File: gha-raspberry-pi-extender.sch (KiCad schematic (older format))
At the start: 1 part

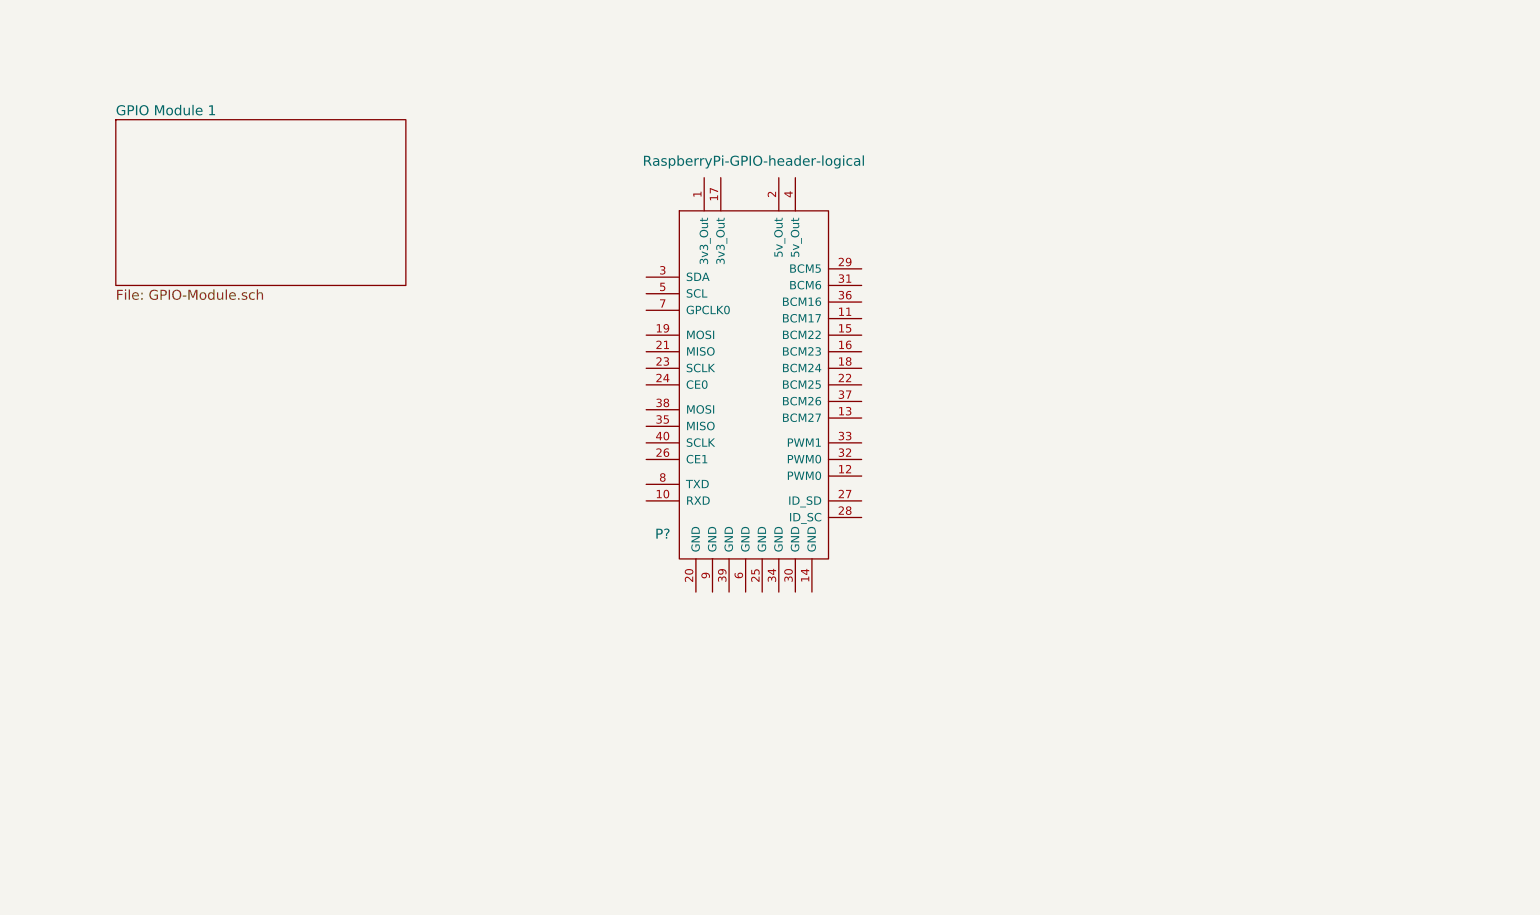
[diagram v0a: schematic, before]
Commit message: finished schematic and started pcb layout
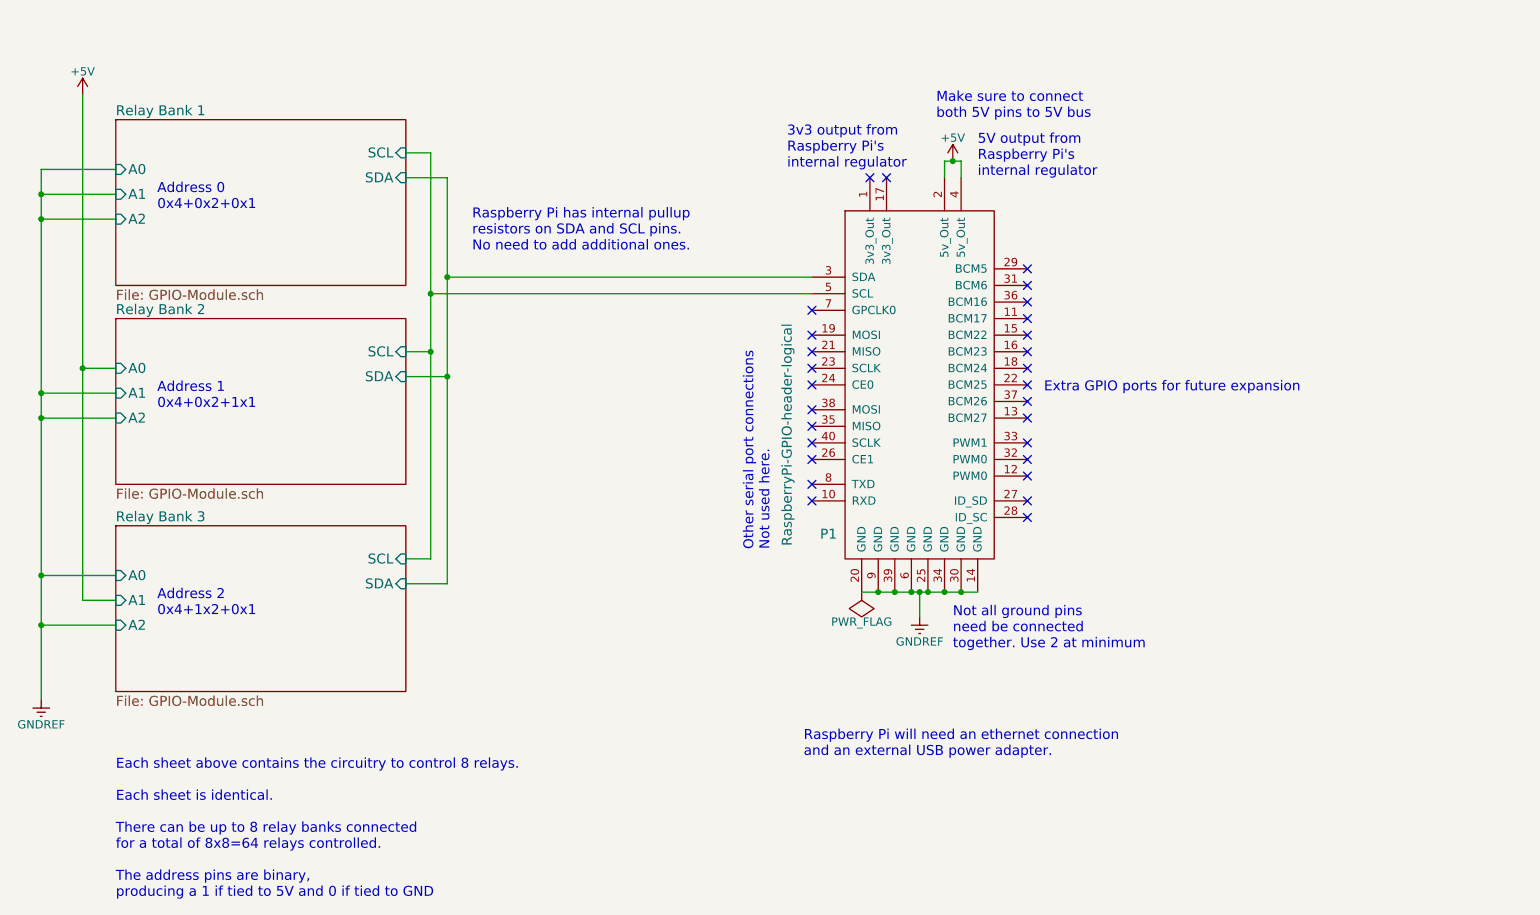
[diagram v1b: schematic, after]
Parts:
- gave numbers to parts that had none: 1
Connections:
- net GNDREF: now reaches P1.14 (GND)
- net GNDREF: now also P1.20 (GND), P1.25 (GND), P1.30 (GND), P1.34 (GND), P1.39 (GND), P1.6 (GND), P1.9 (GND)
- net +5V: now reaches P1.2 (5v_Out)
- net +5V: now also P1.4 (5v_Out)
- net Relay Bank 1/SDA: now reaches P1.3 (SDA)
- net Relay Bank 1/SCL: now reaches P1.5 (SCL)
- no-connect marks 0 -> 28
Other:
- note added: "3v3 output from\nRaspberry Pi's\ninternal regulator"
- note added: "5V output from\nRaspberry Pi's\ninternal regulator"
- note added: "Address 0\n0x4+0x2+0x1"
- note added: "Address 1\n0x4+0x2+1x1"
- note added: "Address 2\n0x4+1x2+0x1"
- note added: "Each sheet above contains the circuitry to control 8 relays.\n\nEach sheet is identical.\n\nThere can be up to 8 relay banks connected\nfor a total of 8x8=64 relays controlled.\n\nThe address pins are binary,\nproducing a 1 if tied to 5V and 0 if tied to GND\n"
- note added: "Extra GPIO ports for future expansion"
- note added: "Make sure to connect\nboth 5V pins to 5V bus"
- note added: "Not all ground pins\nneed be connected\ntogether. Use 2 at minimum"
- note added: "Other serial port connections\nNot used here."
- note added: "Raspberry Pi has internal pullup\nresistors on SDA and SCL pins.\nNo need to add additional ones."
- note added: "Raspberry Pi will need an ethernet connection\nand an external USB power adapter."
- moved on the sheet: P1
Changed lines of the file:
@@
 EELAYER 25 0
 EELAYER END
-$Descr A4 11693 8268
+$Descr USLetter 11000 8500
 encoding utf-8
-Sheet 1 2
-Title ""
-Date ""
+Sheet 1 4
+Title "Main Schematic"
+Date "2016-12-19"
 Rev ""
 Comp ""
@@
 $EndDescr
 $Comp
-L RaspberryPi-GPIO-header-logical P?
+L RaspberryPi-GPIO-header-logical P1
 U 1 1 58586A84
-P 5100 3050
-F 0 "P?" H 4550 2050 60  0000 C CNN
-F 1 "RaspberryPi-GPIO-header-logical" H 5100 4300 60  0000 C CNN
-F 2 "Pin_Headers:Pin_Header_Straight_2x20" H 5100 1500 60  0001 C CNN
-F 3 "http://pinout.xyz/pinout/pijack" H 5150 1600 60  0001 C CNN
-F 4 "0.00@0" H 5000 900 60  0001 C CNN "Pricing"
-F 5 "2x20 pin header" H 5100 1250 60  0001 C CNN "Package ID"
-F 6 "Raspberry Pi" H 4900 1050 60  0001 C CNN "Manufacturer"
-F 7 "Raspberry Pi GPIO headers" H 5000 1150 60  0001 C CNN "Description"
-	1    5100 3050
+P 6100 3050
+F 0 "P1" H 5550 2050 60  0000 C CNN
+F 1 "RaspberryPi-GPIO-header-logical" V 5300 2650 60  0000 C CNN
+F 2 "Pin_Headers:Pin_Header_Straight_2x20" H 6100 1500 60  0001 C CNN
+F 3 "http://pinout.xyz/pinout/pijack" H 6150 1600 60  0001 C CNN
+F 4 "0.00@0" H 6000 900 60  0001 C CNN "Pricing"
+F 5 "2x20 pin header" H 6100 1250 60  0001 C CNN "Package ID"
+F 6 "Raspberry Pi" H 5900 1050 60  0001 C CNN "Manufacturer"
+F 7 "Raspberry Pi GPIO headers" H 6000 1150 60  0001 C CNN "Description"
+	1    6100 3050
 	1    0    0    -1
 $EndComp
@@
 S 1250 1550 1750 1000
 U 58586AAB
-F0 "GPIO Module 1" 60
+F0 "Relay Bank 1" 60
 F1 "GPIO-Module.sch" 60
+F2 "SCL" I R 3000 1750 60
+F3 "SDA" I R 3000 1900 60
+F4 "A0" I L 1250 1850 60
+F5 "A1" I L 1250 2000 60
+F6 "A2" I L 1250 2150 60
 $EndSheet
+$Sheet
+S 1250 2750 1750 1000
+U 58595F89
+F0 "Relay Bank 2" 60
+F1 "GPIO-Module.sch" 60
+F2 "SCL" I R 3000 2950 60
+F3 "SDA" I R 3000 3100 60
+F4 "A0" I L 1250 3050 60
+F5 "A1" I L 1250 3200 60
+F6 "A2" I L 1250 3350 60
+$EndSheet
+$Sheet
+S 1250 4000 1750 1000
+U 58596163
+F0 "Relay Bank 3" 60
+F1 "GPIO-Module.sch" 60
+F2 "SCL" I R 3000 4200 60
+F3 "SDA" I R 3000 4350 60
+F4 "A0" I L 1250 4300 60
+F5 "A1" I L 1250 4450 60
+F6 "A2" I L 1250 4600 60
+$EndSheet
+Text Notes 1250 6250 0    60   ~ 0
+Each sheet above contains the circuitry to control 8 relays.\n\nEach sheet is identical.\n\nThere can be up to 8 relay banks connected\nfor a total of 8x8=64 relays controlled.\n\nThe address pins are binary,\nproducing a 1 if tied to 5V and 0 if tied to GND\n
+Text Notes 3400 2350 0    60   ~ 0
+Raspberry Pi has internal pullup\nresistors on SDA and SCL pins.\nNo need to add additional ones.
+$Comp
+L +5V #PWR01
+U 1 1 58597E7A
+P 6300 1800
+F 0 "#PWR01" H 6300 1650 50  0001 C CNN
+F 1 "+5V" H 6300 1940 50  0000 C CNN
+F 2 "" H 6300 1800 50  0000 C CNN
+F 3 "" H 6300 1800 50  0000 C CNN
+	1    6300 1800
+	1    0    0    -1
+$EndComp
+$Comp
+L GNDREF #PWR02
+U 1 1 58598916
+P 6100 4550
+F 0 "#PWR02" H 6100 4300 50  0001 C CNN
+F 1 "GNDREF" H 6100 4400 50  0000 C CNN
+F 2 "" H 6100 4550 50  0000 C CNN
+F 3 "" H 6100 4550 50  0000 C CNN
+	1    6100 4550
+	1    0    0    -1
+$EndComp
+NoConn ~ 5450 3850
+NoConn ~ 5450 3750
+NoConn ~ 5450 3600
+NoConn ~ 5450 3500
+NoConn ~ 5450 3400
+NoConn ~ 5450 3300
+NoConn ~ 5450 3150
+NoConn ~ 5450 3050
+NoConn ~ 5450 2950
+NoConn ~ 5450 2850
+NoConn ~ 5450 2700
+NoConn ~ 5900 1900
+NoConn ~ 5800 1900
+NoConn ~ 6750 2450
+NoConn ~ 6750 2550
+NoConn ~ 6750 2650
+NoConn ~ 6750 2750
+NoConn ~ 6750 2850
+NoConn ~ 6750 2950
+NoConn ~ 6750 3050
+NoConn ~ 6750 3150
+NoConn ~ 6750 3250
+NoConn ~ 6750 3350
+NoConn ~ 6750 3500
+NoConn ~ 6750 3600
+NoConn ~ 6750 3700
+NoConn ~ 6750 3850
+NoConn ~ 6750 3950
+Text Notes 6450 1900 0    60   ~ 0
+5V output from\nRaspberry Pi's\ninternal regulator
+Text Notes 5300 1850 0    60   ~ 0
+3v3 output from\nRaspberry Pi's\ninternal regulator
+Text Notes 5200 4150 1    60   ~ 0
+Other serial port connections\nNot used here.
+Text Notes 6850 3200 0    60   ~ 0
+Extra GPIO ports for future expansion
+$Comp
+L GNDREF #PWR03
+U 1 1 58599C4C
+P 800 5050
+F 0 "#PWR03" H 800 4800 50  0001 C CNN
+F 1 "GNDREF" H 800 4900 50  0000 C CNN
+F 2 "" H 800 5050 50  0000 C CNN
+F 3 "" H 800 5050 50  0000 C CNN
+	1    800  5050
+	1    0    0    -1
+$EndComp
+$Comp
+L +5V #PWR04
+U 1 1 58599CEA
+P 1050 1400
+F 0 "#PWR04" H 1050 1250 50  0001 C CNN
+F 1 "+5V" H 1050 1540 50  0000 C CNN
+F 2 "" H 1050 1400 50  0000 C CNN
+F 3 "" H 1050 1400 50  0000 C CNN
+	1    1050 1400
+	1    0    0    -1
+$EndComp
+Wire Wire Line
+	3000 1750 3150 1750
+Wire Wire Line
+	3150 1750 3150 4200
+Wire Wire Line
+	3150 2950 3000 2950
+Wire Wire Line
+	3150 4200 3000 4200
+Connection ~ 3150 2950
+Wire Wire Line
+	3000 1900 3250 1900
+Wire Wire Line
+	3250 1900 3250 4350
+Wire Wire Line
+	3250 3100 3000 3100
+Wire Wire Line
+	3250 4350 3000 4350
+Connection ~ 3250 3100
+Wire Wire Line
+	5450 2500 3250 2500
+Connection ~ 3250 2500
+Wire Wire Line
+	5450 2600 3150 2600
+Connection ~ 3150 2600
+Wire Wire Line
+	6250 1800 6350 1800
+Wire Wire Line
+	6250 1800 6250 1900
+Wire Wire Line
+	6350 1800 6350 1900
+Connection ~ 6300 1800
+Wire Wire Line
+	5750 4400 6450 4400
+Connection ~ 5850 4400
+Connection ~ 5950 4400
+Connection ~ 6050 4400
+Connection ~ 6150 4400
+Connection ~ 6250 4400
+Connection ~ 6350 4400
+Wire Wire Line
+	6100 4550 6100 4400
+Connection ~ 6100 4400
+Wire Wire Line
+	800  5050 800  1850
+Wire Wire Line
+	800  1850 1250 1850
+Wire Wire Line
+	1250 2000 800  2000
+Connection ~ 800  2000
+Wire Wire Line
+	1250 2150 800  2150
+Connection ~ 800  2150
+Wire Wire Line
+	1250 3200 800  3200
+Connection ~ 800  3200
+Wire Wire Line
+	1250 3350 800  3350
+Connection ~ 800  3350
+Wire Wire Line
+	1250 4600 800  4600
+Connection ~ 800  4600
+Wire Wire Line
+	1250 4300 800  4300
+Connection ~ 800  4300
+Wire Wire Line
+	1050 1400 1050 4450
+Wire Wire Line
+	1050 3050 1250 3050
+Wire Wire Line
+	1050 4450 1250 4450
+Connection ~ 1050 3050
+Text Notes 1500 2100 0    60   ~ 0
+Address 0\n0x4+0x2+0x1
+Text Notes 1500 3300 0    60   ~ 0
+Address 1\n0x4+0x2+1x1
+Text Notes 1500 4550 0    60   ~ 0
+Address 2\n0x4+1x2+0x1
+Text Notes 5400 5400 0    60   ~ 0
+Raspberry Pi will need an ethernet connection\nand an external USB power adapter.
+Text Notes 6200 1550 0    60   ~ 0
+Make sure to connect\nboth 5V pins to 5V bus
+Text Notes 6300 4750 0    60   ~ 0
+Not all ground pins\nneed be connected\ntogether. Use 2 at minimum
+$Comp
+L PWR_FLAG #FLG05
+U 1 1 5859BA9D
+P 5750 4400
+F 0 "#FLG05" H 5750 4495 50  0001 C CNN
+F 1 "PWR_FLAG" H 5750 4580 50  0000 C CNN
+F 2 "" H 5750 4400 50  0000 C CNN
+F 3 "" H 5750 4400 50  0000 C CNN
+	1    5750 4400
+	-1   0    0    1
+$EndComp
 $EndSCHEMATC

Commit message: fixed some schematic issues
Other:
- note added: "Make sure to connect\nboth 5V pins to 5V bus.\nThis connection exists\nwithin the Raspberry Pi"
- note added: "Not all ground pins\nneed be connected\ntogether externally. \nUse 2 at minimum.\nConnected internally"
- note removed: "Make sure to connect\nboth 5V pins to 5V bus"
- note removed: "Not all ground pins\nneed be connected\ntogether. Use 2 at minimum"
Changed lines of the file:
@@
 LIBS:SW-Microchip
 LIBS:SW-RaspberryPi-GPIO-headers
+LIBS:gha-raspberry-pi-extender-cache
 EELAYER 25 0
 EELAYER END
@@
 Text Notes 5400 5400 0    60   ~ 0
 Raspberry Pi will need an ethernet connection\nand an external USB power adapter.
-Text Notes 6200 1550 0    60   ~ 0
-Make sure to connect\nboth 5V pins to 5V bus
-Text Notes 6300 4750 0    60   ~ 0
-Not all ground pins\nneed be connected\ntogether. Use 2 at minimum
+Text Notes 6300 1550 0    60   ~ 0
+Make sure to connect\nboth 5V pins to 5V bus.\nThis connection exists\nwithin the Raspberry Pi
+Text Notes 6550 4750 0    60   ~ 0
+Not all ground pins\nneed be connected\ntogether externally. \nUse 2 at minimum.\nConnected internally
 $Comp
 L PWR_FLAG #FLG05

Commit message: added relays to control AC voltages
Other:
- note added: "These Flags are just to satisfy\nthe ERC and tell the program\nthat these have power connections"
- note added: "VDD is the DC power\nfor the SPST relays.\nThis will depend on\nexactly what relays are\nused but must be DC"
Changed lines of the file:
@@
 LIBS:SW-Microchip
 LIBS:SW-RaspberryPi-GPIO-headers
+LIBS:SW-gElectroMech
 LIBS:gha-raspberry-pi-extender-cache
 EELAYER 25 0
@@
 Connection ~ 6100 4400
 Wire Wire Line
-	800  5050 800  1850
+	800  1850 800  5050
 Wire Wire Line
 	800  1850 1250 1850
@@
 Not all ground pins\nneed be connected\ntogether externally. \nUse 2 at minimum.\nConnected internally
 $Comp
-L PWR_FLAG #FLG05
-U 1 1 5859BA9D
-P 5750 4400
-F 0 "#FLG05" H 5750 4495 50  0001 C CNN
-F 1 "PWR_FLAG" H 5750 4580 50  0000 C CNN
-F 2 "" H 5750 4400 50  0000 C CNN
-F 3 "" H 5750 4400 50  0000 C CNN
-	1    5750 4400
+L +24V #PWR05
+U 1 1 585B2E62
+P 8100 1800
+F 0 "#PWR05" H 8100 1650 50  0001 C CNN
+F 1 "+24V" H 8100 1940 50  0000 C CNN
+F 2 "" H 8100 1800 50  0000 C CNN
+F 3 "" H 8100 1800 50  0000 C CNN
+	1    8100 1800
+	1    0    0    -1
+$EndComp
+$Comp
+L VDD #PWR06
+U 1 1 585B2F00
+P 8550 1800
+F 0 "#PWR06" H 8550 1650 50  0001 C CNN
+F 1 "VDD" H 8550 1950 50  0000 C CNN
+F 2 "" H 8550 1800 50  0000 C CNN
+F 3 "" H 8550 1800 50  0000 C CNN
+	1    8550 1800
+	1    0    0    -1
+$EndComp
+$Comp
+L PWR_FLAG #FLG07
+U 1 1 585B2F9E
+P 8100 1800
+F 0 "#FLG07" H 8100 1895 50  0001 C CNN
+F 1 "PWR_FLAG" H 8100 1980 50  0000 C CNN
+F 2 "" H 8100 1800 50  0000 C CNN
+F 3 "" H 8100 1800 50  0000 C CNN
+	1    8100 1800
 	-1   0    0    1
 $EndComp
+$Comp
+L PWR_FLAG #FLG08
+U 1 1 585B31A0
+P 8550 1800
+F 0 "#FLG08" H 8550 1895 50  0001 C CNN
+F 1 "PWR_FLAG" H 8550 1980 50  0000 C CNN
+F 2 "" H 8550 1800 50  0000 C CNN
+F 3 "" H 8550 1800 50  0000 C CNN
+	1    8550 1800
+	-1   0    0    1
+$EndComp
+$Comp
+L GNDREF #PWR09
+U 1 1 585B32EE
+P 8850 1800
+F 0 "#PWR09" H 8850 1550 50  0001 C CNN
+F 1 "GNDREF" H 8850 1650 50  0000 C CNN
+F 2 "" H 8850 1800 50  0000 C CNN
+F 3 "" H 8850 1800 50  0000 C CNN
+	1    8850 1800
+	-1   0    0    1
+$EndComp
+$Comp
+L PWR_FLAG #FLG010
+U 1 1 585B34F6
+P 8850 1800
+F 0 "#FLG010" H 8850 1895 50  0001 C CNN
+F 1 "PWR_FLAG" H 8850 1980 50  0000 C CNN
+F 2 "" H 8850 1800 50  0000 C CNN
+F 3 "" H 8850 1800 50  0000 C CNN
+	1    8850 1800
+	-1   0    0    1
+$EndComp
+Text Notes 7800 2300 0    60   ~ 0
+These Flags are just to satisfy\nthe ERC and tell the program\nthat these have power connections
+Text Notes 8450 1400 0    60   ~ 0
+VDD is the DC power\nfor the SPST relays.\nThis will depend on\nexactly what relays are\nused but must be DC
 $EndSCHEMATC
